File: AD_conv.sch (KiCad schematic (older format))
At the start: 30 parts, among them U9 74ACT244PW

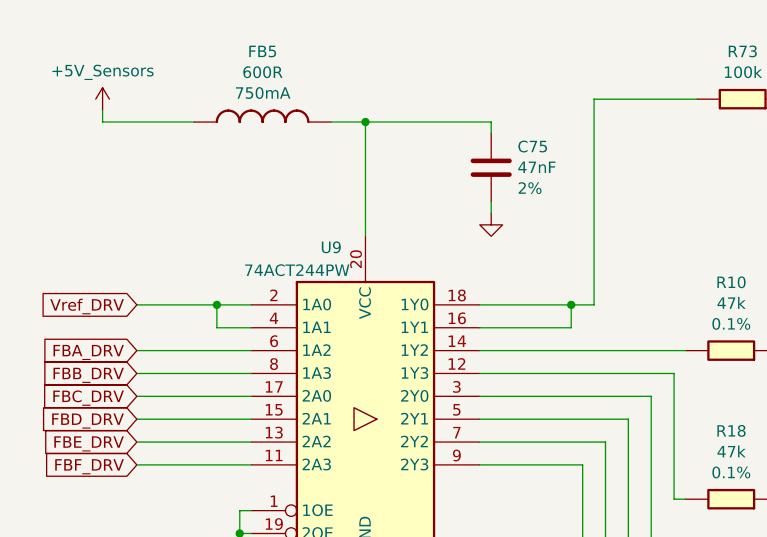
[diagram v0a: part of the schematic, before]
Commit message: Revert "8-way buffer for ADC changed to 74ACT244PW"
This reverts commit 929fdbb6ff0d88cacb7b87749e61dcb260247704.
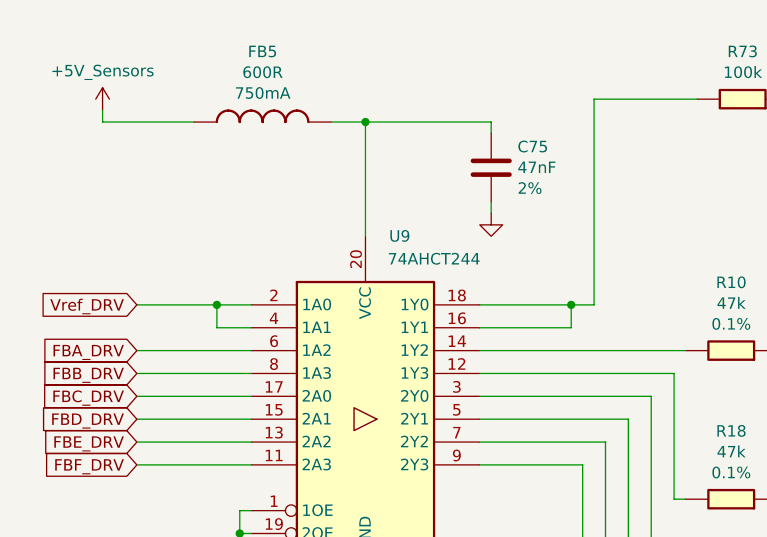
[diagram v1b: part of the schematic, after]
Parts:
- removed U9: 74ACT244PW, symbol OpenVent-rescue:74ACT244PW
- added U9: 74AHCT244, symbol 74xx:74AHCT244
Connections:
- net FBA_DRV: now also U9.6 (1A2)
- net FBB_DRV: now also U9.8 (1A3)
- net FBC_DRV: now also U9.17 (2A0)
- net FBD_DRV: now also U9.15 (2A1)
- net FBE_DRV: now also U9.13 (2A2)
- net FBF_DRV: now also U9.11 (2A3)
- net GND: now also U9.1 (1OE), U9.10 (GND), U9.19 (2OE)
- net Vref_DRV: now also U9.2 (1A0), U9.4 (1A1)
- net at R73.2: now also U9.16 (1Y1), U9.18 (1Y0)
- net at C75.1, FB5.2: now also U9.20 (VCC)
- net at R10.2: now also U9.14 (1Y2)
- net at R18.2: now also U9.12 (1Y3)
- net at R69.2: now also U9.3 (2Y0)
- net at R70.2: now also U9.5 (2Y1)
- net at R71.2: now also U9.7 (2Y2)
- net at R72.2: now also U9.9 (2Y3)
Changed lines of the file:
@@
 $EndDescr
+$Comp
+L 74xx:74AHCT244 U9
+U 1 1 601B9EB9
+P 2650 2300
+F 0 "U9" H 2800 3100 50  0000 C CNN
+F 1 "74AHCT244" H 2950 3000 50  0000 C CNN
+F 2 "" H 2650 2300 50  0001 C CNN
+F 3 "https://assets.nexperia.com/documents/data-sheet/74AHC_AHCT244.pdf" H 2650 2300 50  0001 C CNN
+	1    2650 2300
+	1    0    0    -1
+$EndComp
 $Comp
 L OpenVent:100K_0603_Chip_Resistor,_1%,_0.1W R73
@@
 Wire Wire Line
 	4750 900  4950 900
-$Comp
-L OpenVent-rescue:74ACT244PW U9
-U 1 1 60688267
-P 2650 2300
-F 0 "U9" H 2500 3050 50  0000 C CNN
-F 1 "74ACT244PW" H 2350 2950 50  0000 C CNN
-F 2 "" H 2650 2300 50  0001 C CNN
-F 3 "https://drive.google.com/drive/u/1/folders/1bT0MezjjDfDXdTdQktjf6O5y5oTJs8ND" H 2650 2300 50  0001 C CNN
-	1    2650 2300
-	1    0    0    -1
-$EndComp
 $EndSCHEMATC

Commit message: 8-way buffer for ADC changed to 74ACT244PW
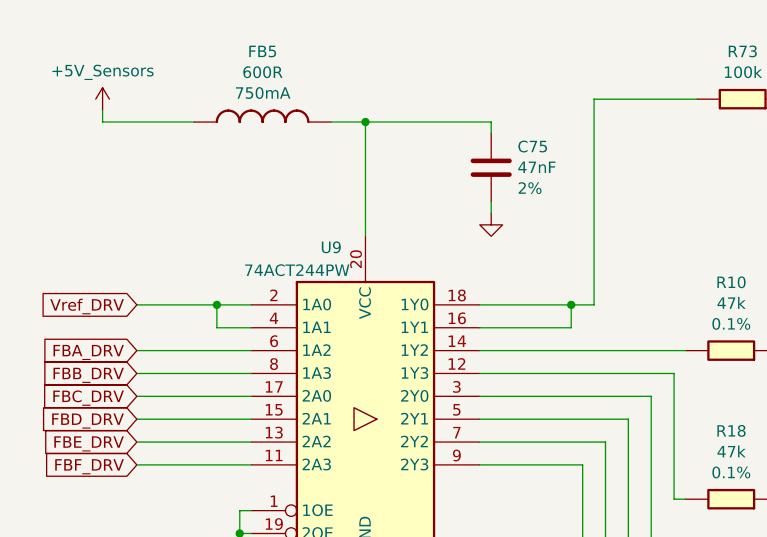
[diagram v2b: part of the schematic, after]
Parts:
- removed U9: 74AHCT244, symbol 74xx:74AHCT244
- added U9: 74ACT244PW, symbol OpenVent-rescue:74ACT244PW
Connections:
- net FBA_DRV: now also U9.6 (1A2)
- net FBB_DRV: now also U9.8 (1A3)
- net FBC_DRV: now also U9.17 (2A0)
- net FBD_DRV: now also U9.15 (2A1)
- net FBE_DRV: now also U9.13 (2A2)
- net FBF_DRV: now also U9.11 (2A3)
- net GND: now also U9.1 (1OE), U9.10 (GND), U9.19 (2OE)
- net Vref_DRV: now also U9.2 (1A0), U9.4 (1A1)
- net at R18.2: now also U9.12 (1Y3)
- net at R10.2: now also U9.14 (1Y2)
- net at R73.2: now also U9.16 (1Y1), U9.18 (1Y0)
- net at C75.1, FB5.2: now also U9.20 (VCC)
- net at R69.2: now also U9.3 (2Y0)
- net at R70.2: now also U9.5 (2Y1)
- net at R71.2: now also U9.7 (2Y2)
- net at R72.2: now also U9.9 (2Y3)
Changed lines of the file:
@@
 $EndDescr
-$Comp
-L 74xx:74AHCT244 U9
-U 1 1 601B9EB9
-P 2650 2300
-F 0 "U9" H 2800 3100 50  0000 C CNN
-F 1 "74AHCT244" H 2950 3000 50  0000 C CNN
-F 2 "" H 2650 2300 50  0001 C CNN
-F 3 "https://assets.nexperia.com/documents/data-sheet/74AHC_AHCT244.pdf" H 2650 2300 50  0001 C CNN
-	1    2650 2300
-	1    0    0    -1
-$EndComp
 $Comp
 L OpenVent:100K_0603_Chip_Resistor,_1%,_0.1W R73
@@
 Wire Wire Line
 	4750 900  4950 900
+$Comp
+L OpenVent-rescue:74ACT244PW U9
+U 1 1 60688267
+P 2650 2300
+F 0 "U9" H 2500 3050 50  0000 C CNN
+F 1 "74ACT244PW" H 2350 2950 50  0000 C CNN
+F 2 "" H 2650 2300 50  0001 C CNN
+F 3 "https://drive.google.com/drive/u/1/folders/1bT0MezjjDfDXdTdQktjf6O5y5oTJs8ND" H 2650 2300 50  0001 C CNN
+	1    2650 2300
+	1    0    0    -1
+$EndComp
 $EndSCHEMATC
